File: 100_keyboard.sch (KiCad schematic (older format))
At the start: 22 parts, among them SW1 SW_Push, U1 MIC5219-3.3YM5, U2 STM32F072RBTx

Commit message: Debug board v0.2
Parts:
- removed C1: 470pF, Capacitor_SMD:C_0805_2012Metric, symbol Device:C_Small
- removed D5: D_Small, Diode_SMD:D_SOD-123, symbol Device:D_Small
- removed U1: MIC5219-3.3YM5, Package_TO_SOT_SMD:SOT-23-5, symbol Regulator_Linear:MIC5219-3.3YM5
- added C2: 22uF 6.3V, Capacitor_SMD:C_0805_2012Metric, symbol Device:C_Small
- added C3: 22nF, Capacitor_SMD:C_0805_2012Metric, symbol Device:C_Small
- added D5: D_Schottky, Diode_SMD:D_SOD-123, symbol Device:D_Schottky
- added D6: 1N4148, Diode_SMD:D_SOD-123, symbol Device:D_Small_ALT
- added L1: 47uH/1.66A, Inductor_SMD:L_2010_5025Metric, symbol Device:L_Small
- added R1: 50kOhm, Resistor_SMD:R_0805_2012Metric, symbol Device:R_Small
- added R4: 100kOhm, Resistor_SMD:R_0805_2012Metric, symbol Device:R_Small
- added R5: 16.2kOhm, Resistor_SMD:R_0805_2012Metric, symbol Device:R_Small
- added U1: mp2359, Package_TO_SOT_SMD:SOT-23-6, symbol random-keyboard-parts:mp2359
- renumbered C3 to C4, C2 to C5, R1 to R0
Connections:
- wire segments 67 -> 65
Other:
- moved on the sheet: C4, C5, C6, C7

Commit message: Debug Board v0.3
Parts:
- added D10, D11, D12, D13, D14, D9: WS2812B, LED_SMD:LED_WS2812B_PLCC4_5.0x5.0mm_P3.2mm, symbol LED:WS2812B
- added D7, D8: D_Small, Diode_SMD:D_SOD-123, symbol Device:D_Small
- added J1: Conn_01x04, Connector_PinHeader_2.54mm:PinHeader_1x04_P2.54mm_Vertical, symbol Connector_Generic:Conn_01x04
- added J2: Conn_01x03, Connector_PinHeader_1.27mm:PinHeader_1x03_P1.27mm_Vertical, symbol Connector_Generic:Conn_01x03
- added MX5, MX6: MX-NoLED, MX_Alps_Hybrid:MX-1U, symbol 100_keyboard-rescue:MX-NoLED-MX_Alps_Hybrid
- L1: footprint Inductor_SMD:L_2010_5025Metric -> Inductor_SMD:L_10.4x10.4_H4.8
- MX1, MX2, MX3, MX4: symbol MX_Alps_Hybrid:MX-NoLED -> 100_keyboard-rescue:MX-NoLED-MX_Alps_Hybrid
- U1: symbol random-keyboard-parts:mp2359 -> 100_keyboard-rescue:mp2359-random-keyboard-parts
- USB1: symbol random-keyboard-parts:Molex-0548190589 -> 100_keyboard-rescue:Molex-0548190589-random-keyboard-parts
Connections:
- net labels added: COL2, LED_SPI, SWDCLK, SWDIO
- wire segments 65 -> 108
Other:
- moved on the sheet: C2, C3, C4, C5, C6, C7, D5, D6, L1, R1, R4, R5

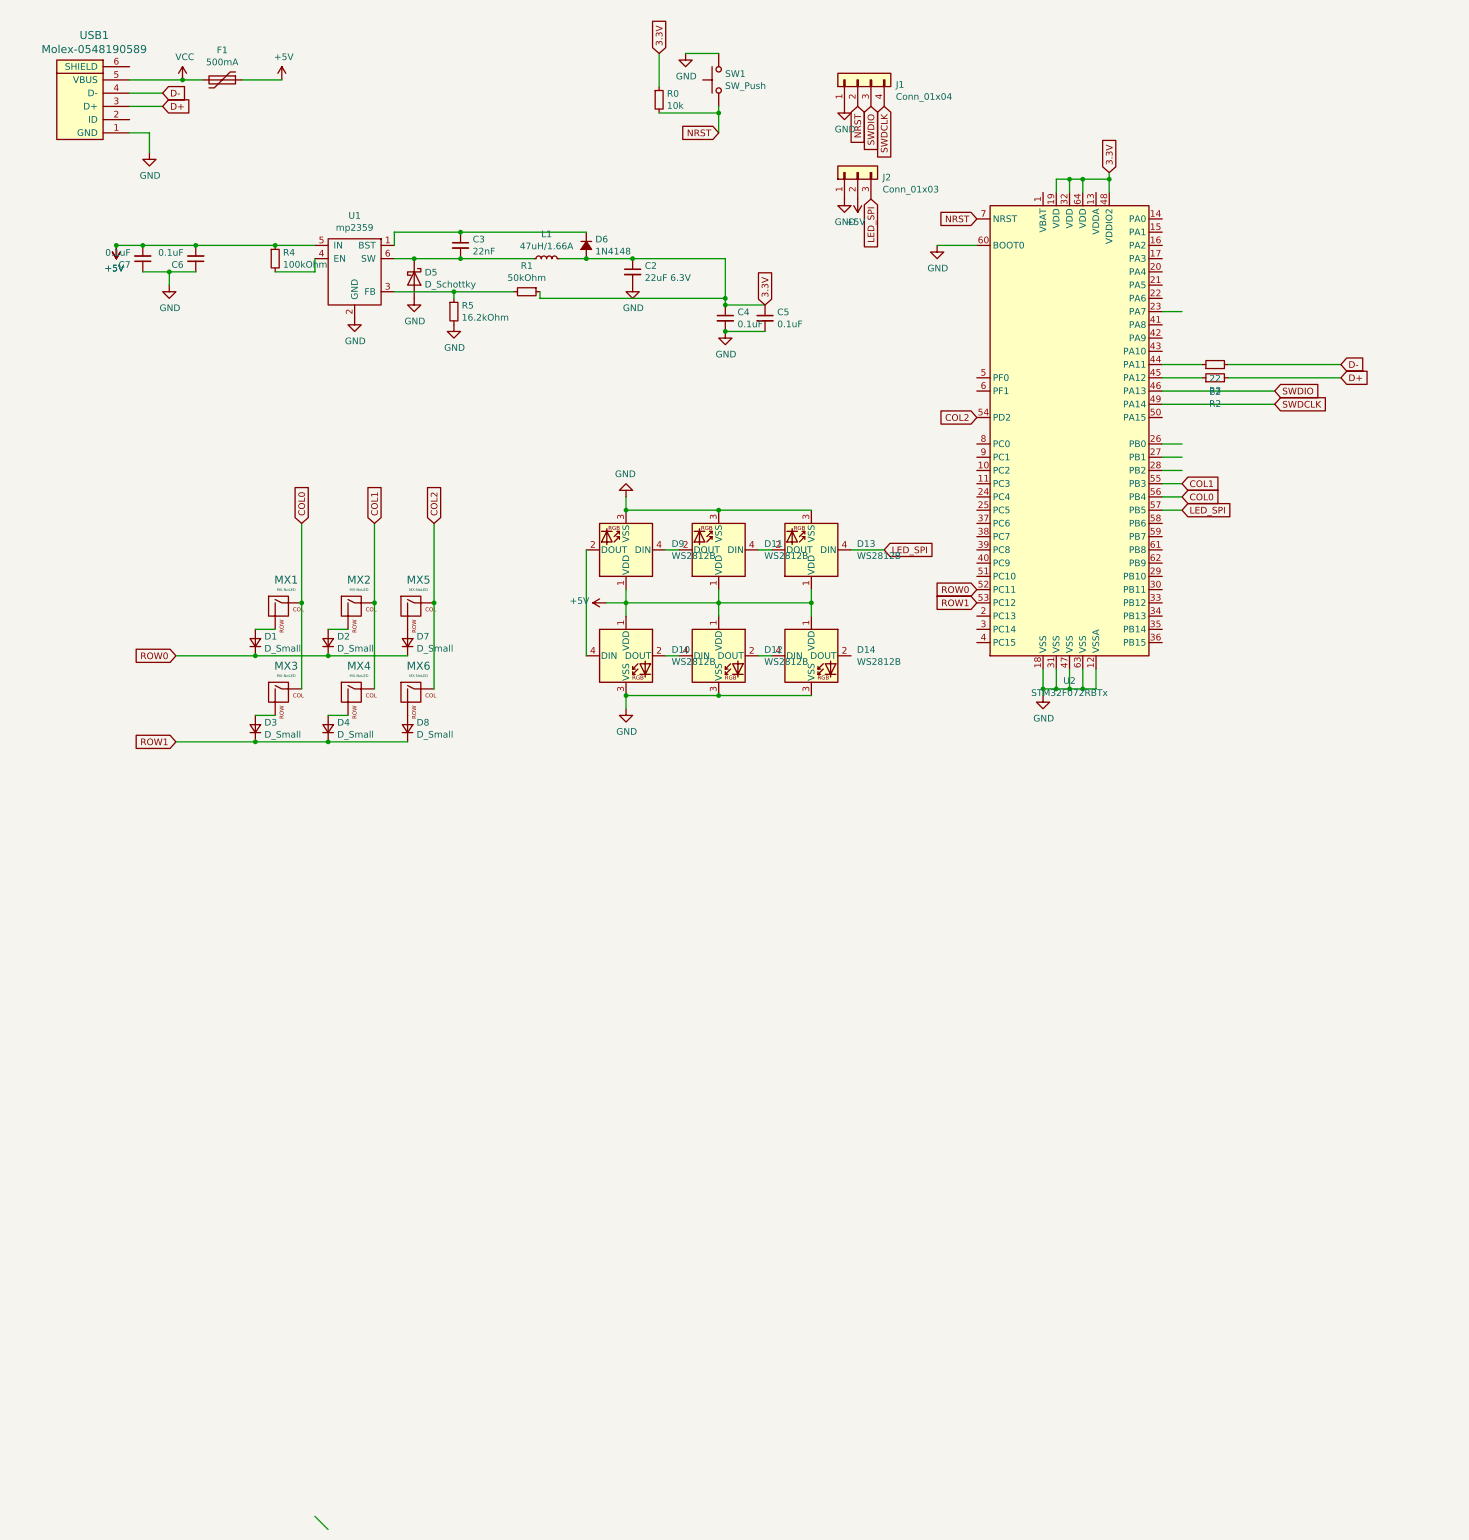
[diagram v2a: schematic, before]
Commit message: Debug board v0.4 beginnings
Signed-off-by: localcc <work@zloserver.com>
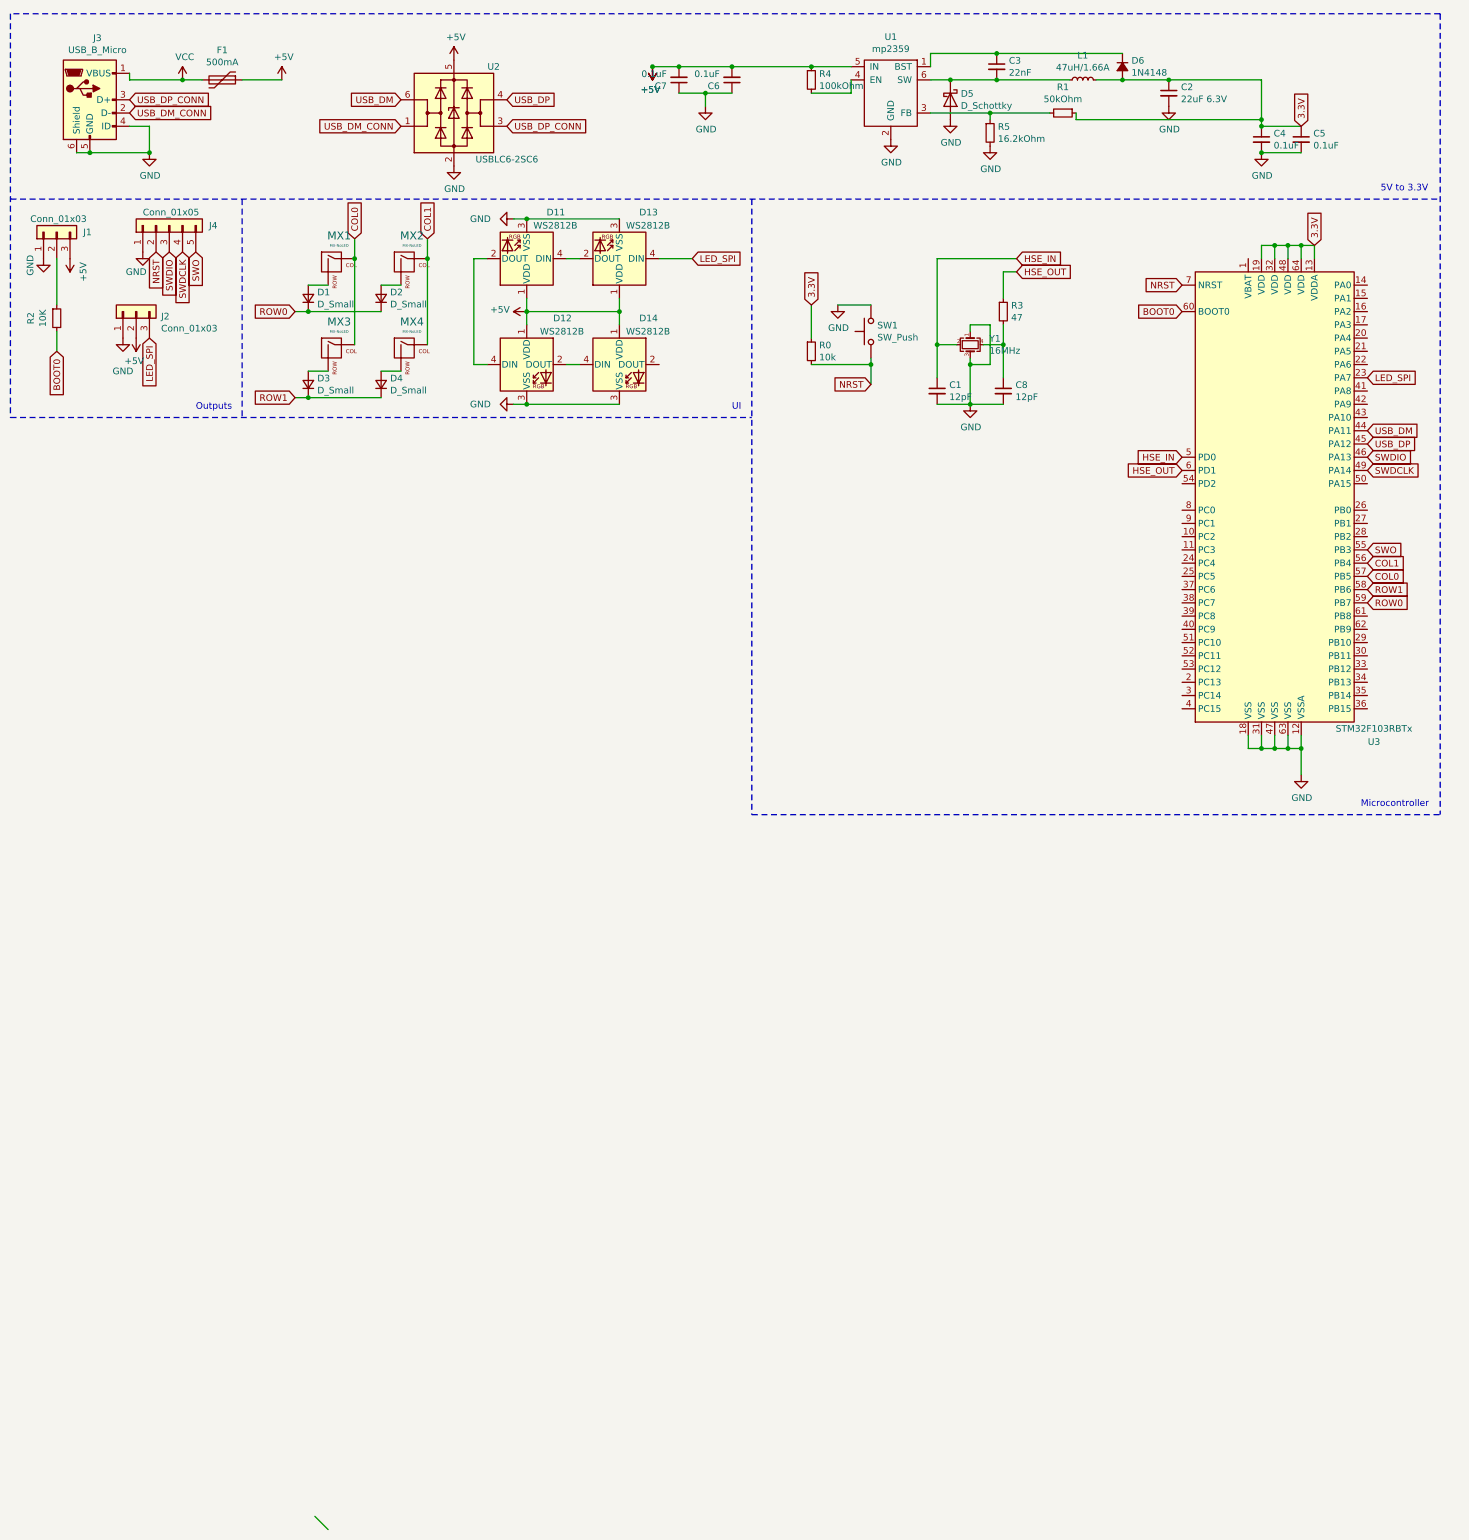
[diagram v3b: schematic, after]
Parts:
- removed D10, D9: WS2812B, LED_SMD:LED_WS2812B_PLCC4_5.0x5.0mm_P3.2mm, symbol LED:WS2812B
- removed D7, D8: D_Small, Diode_SMD:D_SOD-123, symbol Device:D_Small
- removed J1: Conn_01x04, Connector_PinHeader_2.54mm:PinHeader_1x04_P2.54mm_Vertical, symbol Connector_Generic:Conn_01x04
- removed MX5, MX6: MX-NoLED, MX_Alps_Hybrid:MX-1U, symbol 100_keyboard-rescue:MX-NoLED-MX_Alps_Hybrid
- removed U2: STM32F072RBTx, Package_QFP:LQFP-64_10x10mm_P0.5mm, symbol MCU_ST_STM32F0:STM32F072RBTx
- removed USB1: Molex-0548190589, random-keyboard-parts:Molex-0548190589, symbol 100_keyboard-rescue:Molex-0548190589-random-keyboard-parts
- added C1, C8: 12pF, Capacitor_SMD:C_0805_2012Metric, symbol Device:C_Small
- added J1: Conn_01x03, Connector_PinHeader_1.27mm:PinHeader_1x03_P1.27mm_Vertical, symbol Connector_Generic:Conn_01x03
- added J3: USB_B_Micro, Connector_USB:USB_Micro-B_Molex_47346-0001, symbol Connector:USB_B_Micro
- added J4: Conn_01x05, Connector_PinHeader_1.27mm:PinHeader_1x05_P1.27mm_Vertical, symbol Connector_Generic:Conn_01x05
- added U2: USBLC6-2SC6, Package_TO_SOT_SMD:SOT-23-6, symbol Power_Protection:USBLC6-2SC6
- added U3: STM32F103RBTx, Package_QFP:LQFP-64_10x10mm_P0.5mm, symbol MCU_ST_STM32F1:STM32F103RBTx
- added Y1: 16MHz, Crystal:Crystal_SMD_5032-4Pin_5.0x3.2mm, symbol Device:Crystal_GND24_Small
- R2: value 22 -> 10K
- R3: value 22 -> 47
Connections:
- net labels added: BOOT0, HSE_IN, HSE_OUT, SWO, USB_DM, USB_DM_CONN, USB_DP, USB_DP_CONN
- net labels removed: COL2, D+, D-
- wire segments 108 -> 105
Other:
- note added: "5V to 3.3V\n"
- note added: "Microcontroller\n"
- note added: "Outputs\n"
- note added: "UI\n"
- moved on the sheet: C2, C3, C4, C5, C6, C7, D1, D11, D12, D13, D14, D2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
